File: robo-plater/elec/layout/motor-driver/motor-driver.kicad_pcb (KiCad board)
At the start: 2 copper layers, 12 parts, among them U1 ?, U2 ?, U3 ?

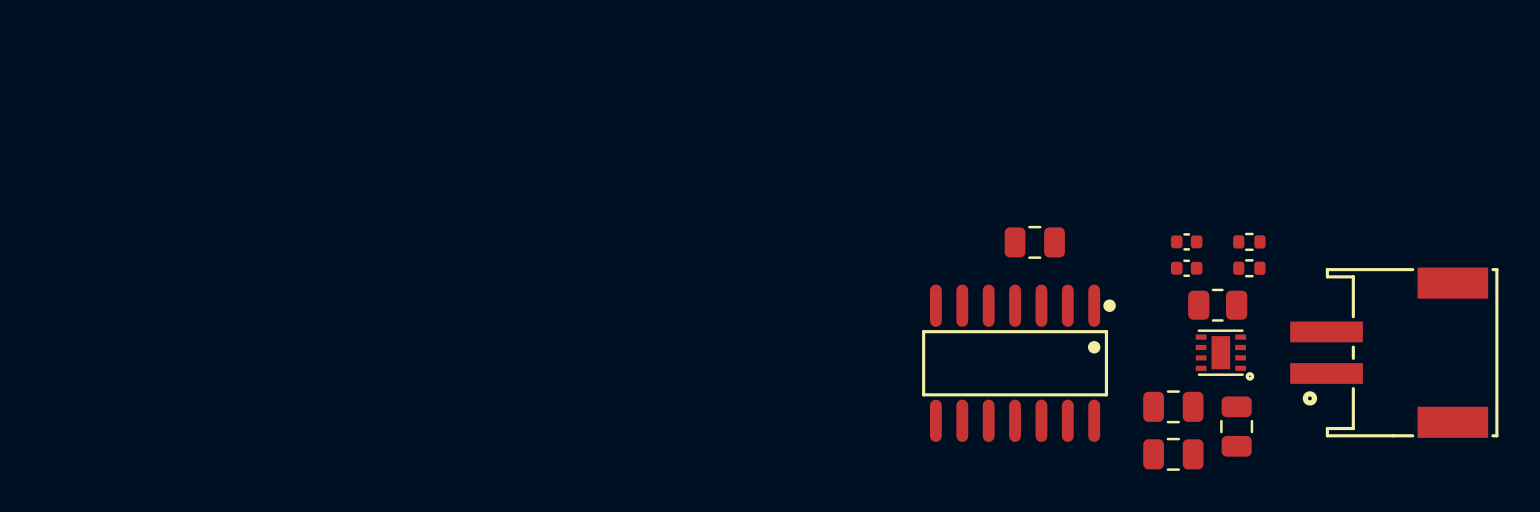
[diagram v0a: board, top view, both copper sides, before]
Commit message: Update feedback circuit
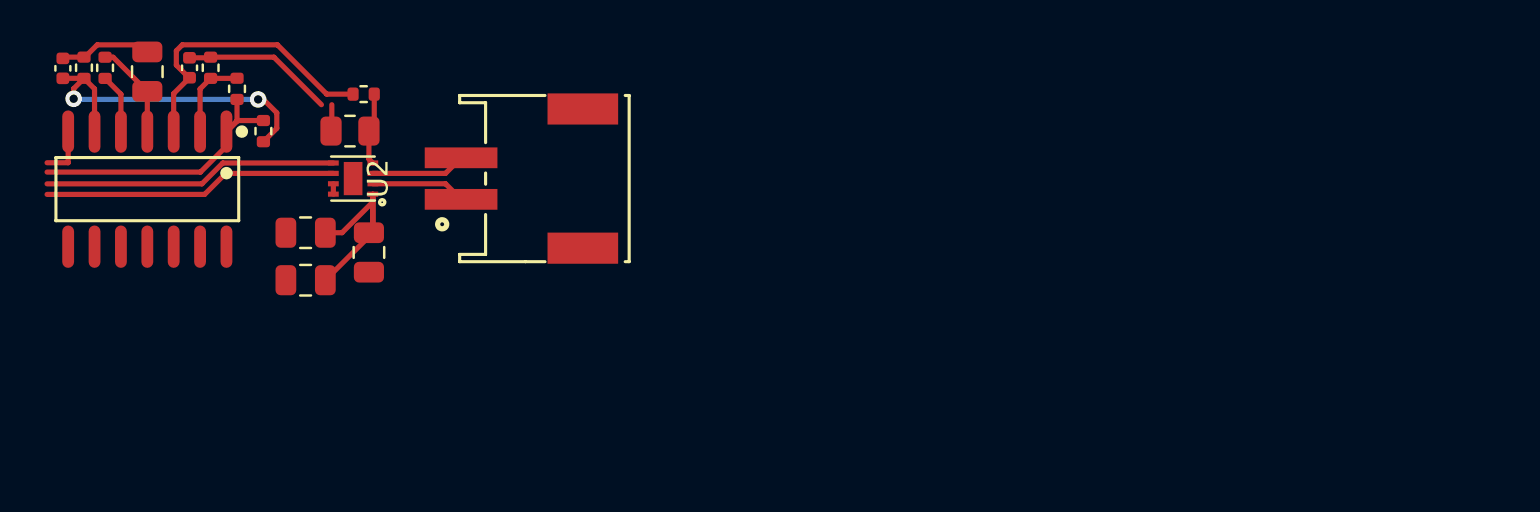
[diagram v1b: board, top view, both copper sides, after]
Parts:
- added R3: 62.5mW Thick Film Resistors 50V ±100ppm/℃ ±1% 365Ω 0402 Chi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, lib:R0402, F.Cu at (124.6, 67.3)
- added R4: 62.5mW Thick Film Resistors 50V ±100ppm/℃ ±1% 36.5Ω 0402 Ch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, lib:R0402, F.Cu at (123.3, 66.3)
- added R6: 62.5mW Thick Film Resistors 50V ±100ppm/℃ ±1% 1MΩ 0402 Chip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, lib:R0402, F.Cu at (118.2, 66.3)
- added R7: 62.5mW Thick Film Resistors 50V ±100ppm/℃ ±1% 1MΩ 0402 Chip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, lib:R0402, F.Cu at (117.2, 66.3)
- moved C6 54.7 mm to (116.2, 66.3), turned to 90 degrees
- moved C5 49.0 mm to (122.3, 66.3), turned to 90 degrees
- moved R5 47.8 mm to (125.9, 69.3), turned to -90 degrees
- moved C4 43.5 mm to (120.3, 66.5), turned to 90 degrees
- moved R2 43.4 mm to (130.7, 67.6)
- moved C3 42.6 mm to (130.9, 75.2)
- moved R1 42.6 mm to (130.0, 69.3)
- moved U1 42.6 mm to (130.2, 71.6)
- moved U2 42.6 mm to (138.3, 71.6)
- moved C1 42.6 mm to (127.9, 76.5)
- moved C2 42.6 mm to (127.9, 74.2)
- moved U3 42.6 mm to (120.3, 72.1)
- renumbered R3 to R5
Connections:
- net op_amp-out2 renamed pulses
- C6 pad 1: in1_minus -> in2_minus
- R5 pad 1: _shunt_high -> current
- R5 pad 2: in1_minus -> in2_minus
- U1 pad 3: driver-out2 -> out2
- U3 pad 1: feedback -> current
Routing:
- net in2_minus: track 0.00 -> 16.7 mm, vias 0 -> 2
- net dir: track 0.00 -> 14.2 mm
- net pwm: track 0.00 -> 14.2 mm
- net in1_plus: track 0.00 -> 14.1 mm
- net current: track 0.00 -> 13.6 mm
- net gnd: track 0.00 -> 13.1 mm
- net vcc: track 0.00 -> 10.0 mm
- net out1: track 0.00 -> 9.12 mm
- net vcc-1: track 0.00 -> 5.15 mm
- net in1_minus: track 0.00 -> 4.04 mm
- net _shunt_high: track 0.00 -> 3.50 mm
- net in2_plus: track 0.00 -> 2.88 mm
- net pulses: track 0.00 -> 2.52 mm

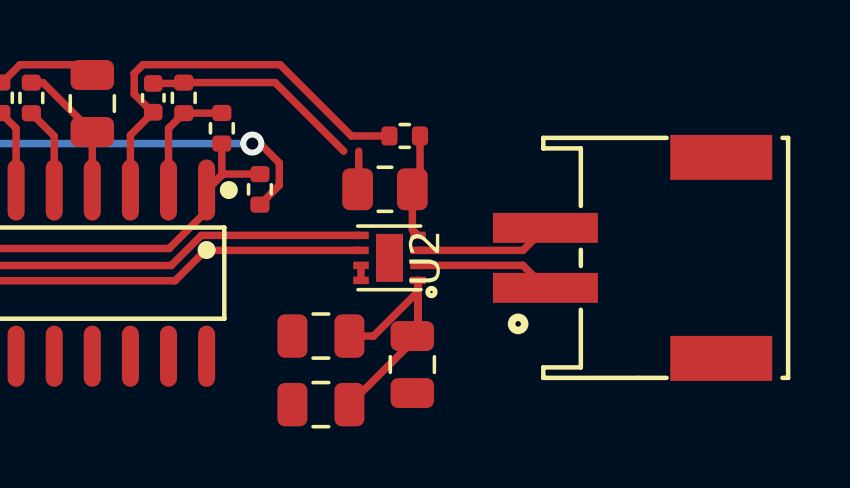
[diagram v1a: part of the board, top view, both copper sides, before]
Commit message: Two motor driver channels with debug headers
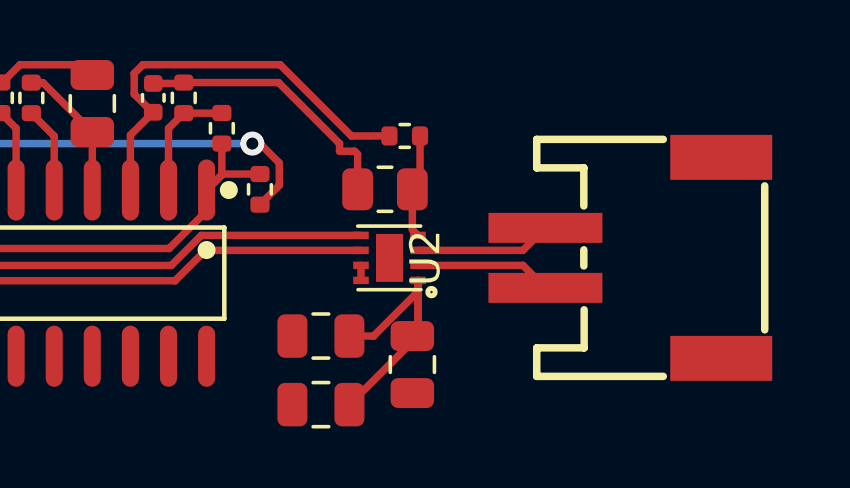
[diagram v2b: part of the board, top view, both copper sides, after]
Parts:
- added U3: ?, lib:NetTie-2_SMD_Pad0.25mm, F.Cu at (128.5, 68.1)
- U2: footprint lib:CONN-SMD_PH-2AWB -> lib:CONN-SMD_P2.00_S2B-PH-SM4-TB-LF-SN
- renumbered U3 to U4
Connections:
- C5 pad 2: gnd -> _shunt_gnd
- R4 pad 2: gnd -> _shunt_gnd
- U2 pad 2: driver-out2 -> out2
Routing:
- net _shunt_gnd: track 0.00 -> 7.32 mm
- net gnd: track 13.1 -> 5.84 mm
- net out2: track 0.00 -> 4.56 mm
- net out1: track 9.12 -> 4.56 mm

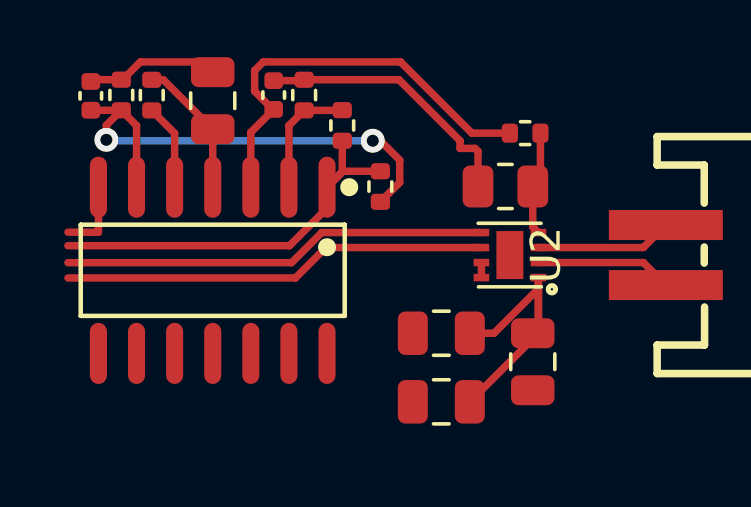
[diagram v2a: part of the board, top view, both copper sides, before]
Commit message: Add stemma/quuic connectors and load cell amps
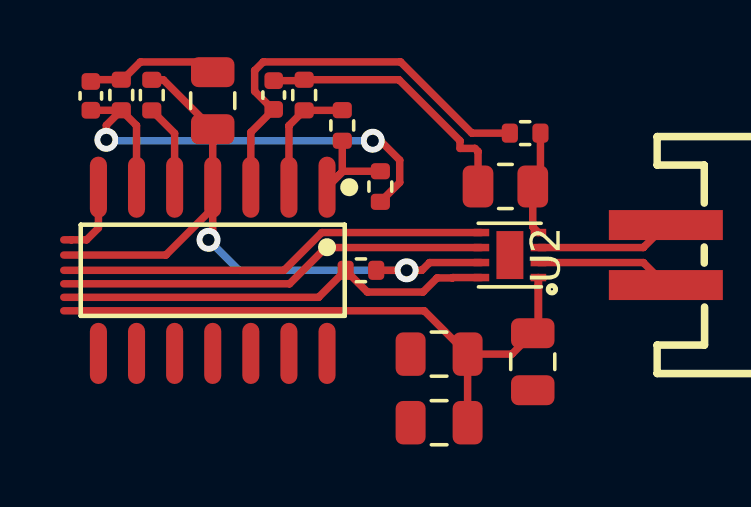
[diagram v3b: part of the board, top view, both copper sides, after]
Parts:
- added R1: 62.5mW Thick Film Resistors 50V ±100ppm/℃ ±1% 10kΩ 0402 Chi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, lib:R0402, F.Cu at (125.2, 72.1)
- moved C2 0.70 mm to (127.8, 74.9)
- moved C1 0.70 mm to (127.8, 77.2)
- renumbered R1 to R2, R2 to R3, R3 to R4, R4 to R5, R5 to R6, R6 to R7, R7 to R8
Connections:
- U1 pad 8: vcc-1 -> enable
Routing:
- net vcc-1: track 5.15 -> 23.4 mm, vias 0 -> 2
- net enable: track 0.00 -> 14.8 mm
- net vcc: track 10.0 -> 22.7 mm
- net current: track 13.6 -> 4.46 mm
